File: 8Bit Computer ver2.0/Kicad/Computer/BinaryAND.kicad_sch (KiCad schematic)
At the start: 4 parts, among them IC22 SN74LVC1G14DBVR, IC24 SN74ABT574ADWR, IC28 SN74LVC1G08DBVR, IC6 SN74AHC74DR

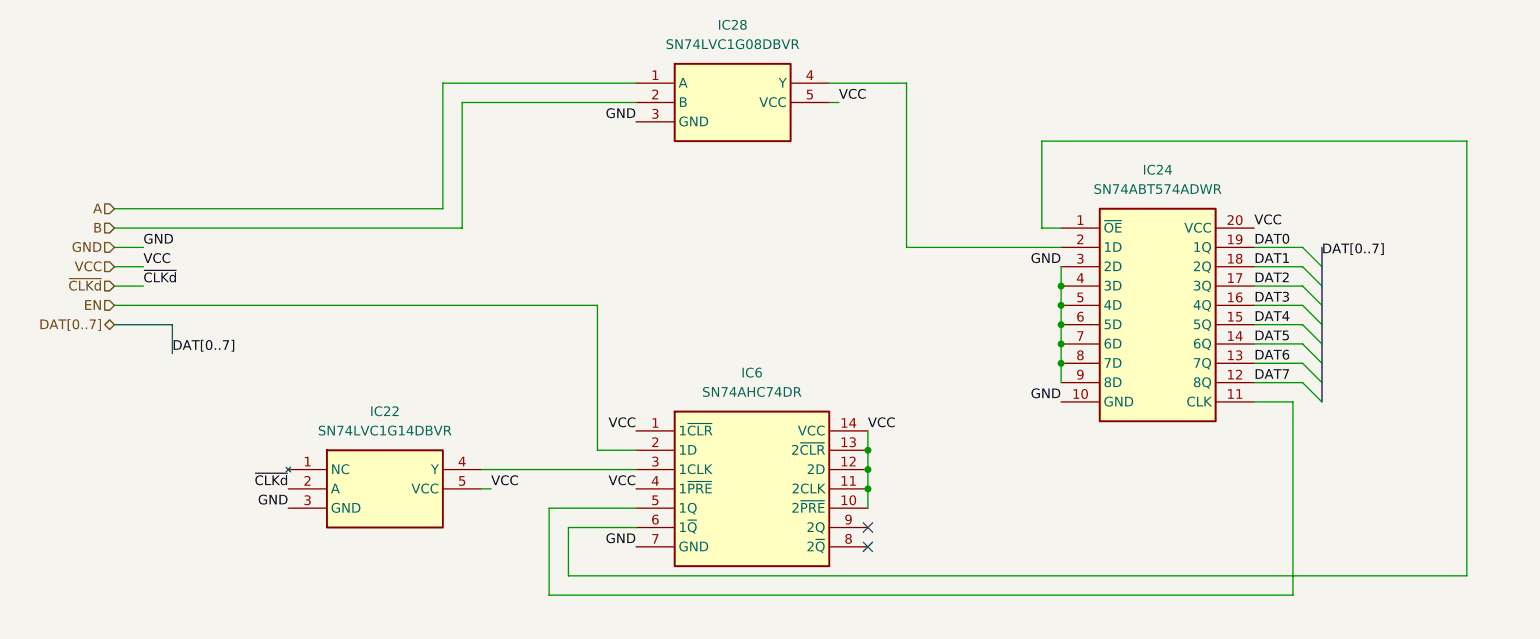
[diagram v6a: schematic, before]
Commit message: Kicad SCH/PCB
Kicad SCH/PCB:
changed the References in SCH
began with INOUTPUT module nearly done
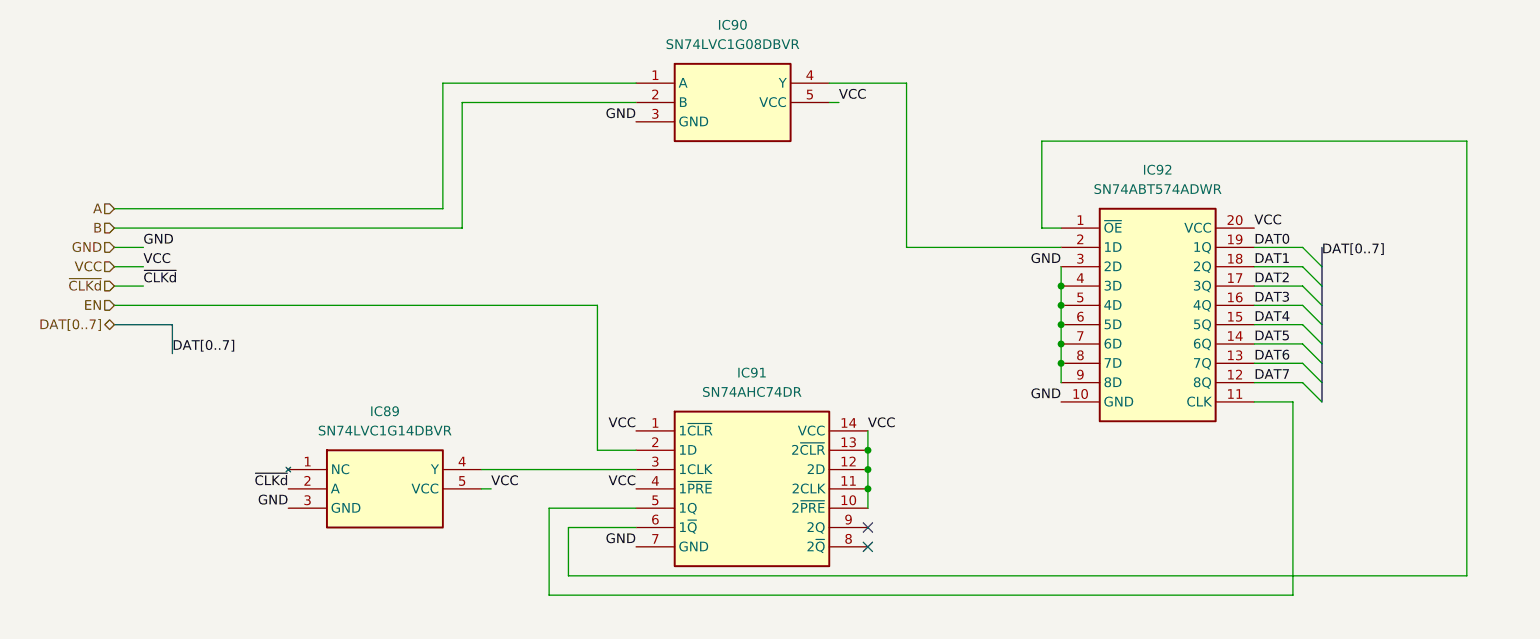
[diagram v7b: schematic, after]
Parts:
- renumbered IC22 to IC89, IC28 to IC90, IC6 to IC91, IC24 to IC92
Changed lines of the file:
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@@
 		(dnp no)
 		(fields_autoplaced yes)
-		(property "Reference" "IC6"
+		(property "Reference" "IC91"
 			(at 123.19 93.98 0)
 			(effects
@@
 			(project "Computer"
 				(path "/1196a00e-6878-4d6d-82b7-9e052dfe7c14/c4d8b530-1c6d-45af-88d2-7dc1d4321a34/aefbc185-b96a-4e68-9567-15494077fa52"
-					(reference "IC6")
+					(reference "IC91")
 					(unit 1)
 				)
@@
 		(dnp no)
 		(fields_autoplaced yes)
-		(property "Reference" "IC24"
+		(property "Reference" "IC92"
 			(at 176.53 67.31 0)
 			(effects
@@
 			(project "Computer"
 				(path "/1196a00e-6878-4d6d-82b7-9e052dfe7c14/c4d8b530-1c6d-45af-88d2-7dc1d4321a34/aefbc185-b96a-4e68-9567-15494077fa52"
-					(reference "IC24")
+					(reference "IC92")
 					(unit 1)
 				)
@@
 		(dnp no)
 		(fields_autoplaced yes)
-		(property "Reference" "IC22"
+		(property "Reference" "IC89"
 			(at 74.93 99.06 0)
 			(effects
@@
 			(project "Computer"
 				(path "/1196a00e-6878-4d6d-82b7-9e052dfe7c14/c4d8b530-1c6d-45af-88d2-7dc1d4321a34/aefbc185-b96a-4e68-9567-15494077fa52"
-					(reference "IC22")
+					(reference "IC89")
 					(unit 1)
 				)
@@
 		(dnp no)
 		(fields_autoplaced yes)
-		(property "Reference" "IC28"
+		(property "Reference" "IC90"
 			(at 120.65 48.26 0)
 			(effects
@@
 			(project "Computer"
 				(path "/1196a00e-6878-4d6d-82b7-9e052dfe7c14/c4d8b530-1c6d-45af-88d2-7dc1d4321a34/aefbc185-b96a-4e68-9567-15494077fa52"
-					(reference "IC28")
+					(reference "IC90")
 					(unit 1)
 				)
